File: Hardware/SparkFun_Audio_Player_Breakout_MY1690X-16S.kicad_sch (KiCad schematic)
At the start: 41 parts, among them J1 3.5mm TRRS, J2 Conn_01x03, J3 Conn_01x02, J4 USB_C_Receptacle, J5 Conn_01x06, J6 microSD, Q1 BSS138, U2 MY1690X-16S

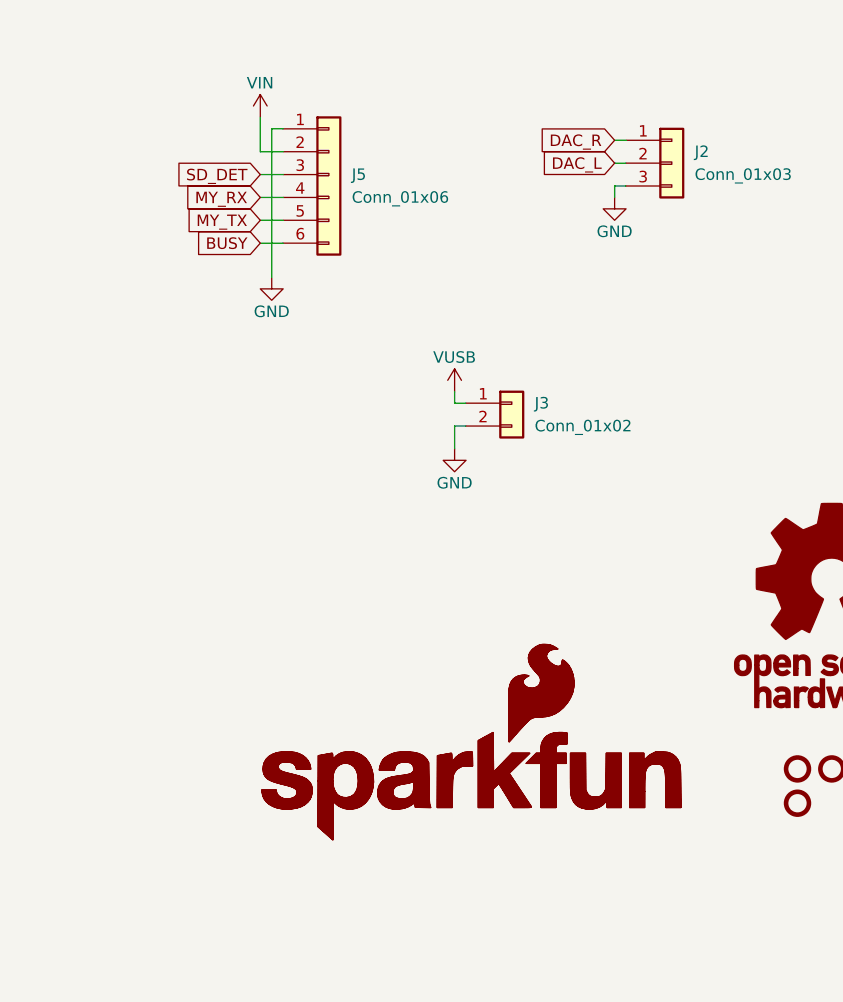
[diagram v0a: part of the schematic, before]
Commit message: re-order header pins to put GND/VIN/RX/TX in a row
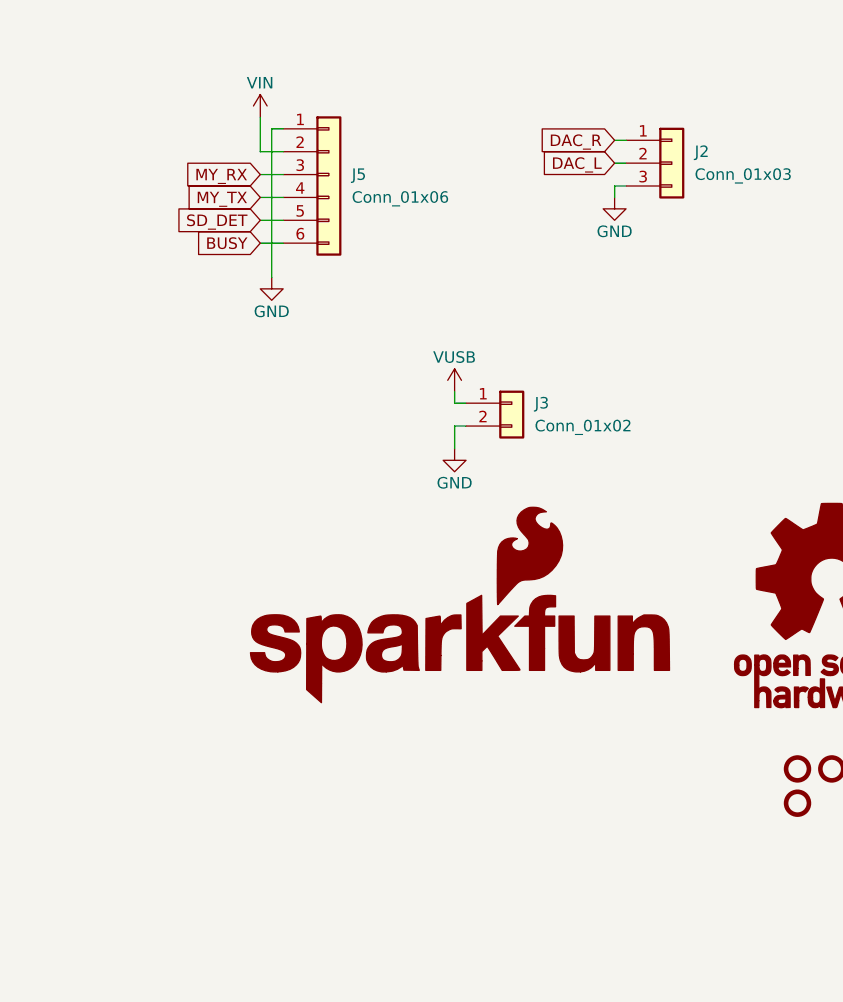
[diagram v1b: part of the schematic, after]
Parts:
- removed G3: SparkFun_Logo, symbol SparkFun-Aesthetic:SparkFun_Logo
- removed J1: 3.5mm TRRS, SparkFun-Connector:Audio_Jack_3.5mm_TRRS_SMD_RA, symbol SparkFun-Connector:Audio Jack TRRS 3.5mm SMD
- added J1: 3.5mm TRRS, SparkFun-Connector:Audio_Jack_3.5mm_TRRS_SMD_RA, symbol SparkFun-Connector:Audio_Jack_TRRS_3.5mm_SMD
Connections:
- net DAC_L: now also J1.T
- net DAC_R: now also J1.R1
- net GND: now also J1.R2
- net MY_RX: now also J5.3 (Pin_3); no longer J5.4 (Pin_4)
- net MY_TX: now also J5.4 (Pin_4); no longer J5.5 (Pin_5)
- net SD_DET: now also J5.5 (Pin_5); no longer J5.3 (Pin_3)
- net at JP3.1 (A): now also J1.S
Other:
- title: SparkFun Serial MP3 Player Shield -> SparkFun Audio Player Breakout MY1690X-16S
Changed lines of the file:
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@@
 	(paper "USLetter")
 	(title_block
-		(title "SparkFun Serial MP3 Player Shield")
-		(date "2025-01-17")
-		(rev "v11")
-		(comment 1 "Designed by: N. Seidle")
+		(title "SparkFun Audio Player Breakout MY1690X-16S")
+		(date "2025-01-24")
+		(rev "v01")
+		(comment 1 "Designed by: P. Lewis")
+		(comment 2 "Based on the MP3 Trigger Shield R3 by N. Seidle")
 	)
 	(junction
@@
 		)
 	)
+	(global_label "SD_DET"
+		(shape input)
+		(at 189.23 116.84 180)
+		(fields_autoplaced yes)
+		(effects
+			(font
+				(size 1.27 1.27)
+			)
+			(justify right)
+		)
+		(property "Intersheetrefs" "${INTERSHEET_REFS}"
+			(at 179.4111 116.84 0)
+			(effects
+				(font
+					(size 1.27 1.27)
+				)
+				(justify right)
+				(hide yes)
+			)
+		)
+	)
 	(global_label "MY_RX_LV"
 		(shape input)
@@
 		)
 	)
-	(global_label "SD_DET"
+	(global_label "MY_TX"
 		(shape input)
-		(at 189.23 111.76 180)
+		(at 189.23 114.3 180)
 		(fields_autoplaced yes)
 		(effects
@@
 		)
 		(property "Intersheetrefs" "${INTERSHEET_REFS}"
-			(at 179.4111 111.76 0)
+			(at 180.5601 114.3 0)
 			(effects
 				(font
@@
 	(global_label "MY_RX"
 		(shape input)
-		(at 189.23 114.3 180)
+		(at 189.23 111.76 180)
 		(fields_autoplaced yes)
 		(effects
@@
 		)
 		(property "Intersheetrefs" "${INTERSHEET_REFS}"
-			(at 180.2577 114.3 0)
+			(at 180.2577 111.76 0)
 			(effects
 				(font
@@
 		)
 	)
-	(global_label "MY_TX"
-		(shape input)
-		(at 189.23 116.84 180)
-		(fields_autoplaced yes)
-		(effects
-			(font
-				(size 1.27 1.27)
-			)
-			(justify right)
-		)
-		(property "Intersheetrefs" "${INTERSHEET_REFS}"
-			(at 180.5601 116.84 0)
-			(effects
-				(font
-					(size 1.27 1.27)
-				)
-				(justify right)
-				(hide yes)
-			)
-		)
-	)
 	(global_label "DAC_R"
 		(shape input)
@@
 	)
 	(symbol
+		(lib_id "SparkFun-Connector:Audio_Jack_TRRS_3.5mm_SMD")
+		(at 57.15 111.76 0)
+		(mirror y)
+		(unit 1)
+		(exclude_from_sim no)
+		(in_bom yes)
+		(on_board yes)
+		(dnp no)
+		(property "Reference" "J1"
+			(at 59.69 102.87 0)
+			(effects
+				(font
+					(size 1.27 1.27)
+				)
+			)
+		)
+		(property "Value" "3.5mm TRRS"
+			(at 59.69 105.41 0)
+			(effects
+				(font
+					(size 1.27 1.27)
+				)
+			)
+		)
+		(property "Footprint" "SparkFun-Connector:Audio_Jack_3.5mm_TRRS_SMD_RA"
+			(at 57.15 123.19 0)
+			(effects
+				(font
+					(size 1.27 1.27)
+				)
+				(hide yes)
+			)
+		)
+		(property "Datasheet" "https://cdn.sparkfun.com/datasheets/Prototyping/20153.pdf"
+			(at 57.15 120.65 0)
+			(effects
+				(font
+					(size 1.27 1.27)
+				)
+				(hide yes)
+			)
+		)
+		(property "Description" "Audio Jack, 4 Poles (TRRS)"
+			(at 57.15 125.73 0)
+			(effects
+				(font
+					(size 1.27 1.27)
+				)
+				(hide yes)
+			)
+		)
+		(property "PROD_ID" "CONN-10676"
+			(at 57.15 128.27 0)
+			(effects
+				(font
+					(size 1.27 1.27)
+				)
+				(hide yes)
+			)
+		)
+		(pin "S"
+		)
+		(pin "T"
+		)
+		(pin "R2"
+		)
+		(pin "R1"
+		)
+		(instances
+			(project ""
+				(path "/e3dd3ae4-244d-4cba-9cca-5d2abf83f29a"
+					(reference "J1")
+					(unit 1)
+				)
+			)
+		)
+	)
+	(symbol
 		(lib_id "SparkFun-PowerSymbol:3.3V_P")
 		(at 119.38 111.76 0)
@@
 	(symbol
 		(lib_id "SparkFun-Aesthetic:SparkFun_Logo")
-		(at 212.09 179.07 0)
+		(at 210.82 163.83 0)
 		(unit 1)
 		(exclude_from_sim no)
@@
 		(fields_autoplaced yes)
 		(property "Reference" "G5"
-			(at 212.09 172.72 0)
+			(at 210.82 157.48 0)
 			(effects
 				(font
@@
 		)
 		(property "Value" "SparkFun_Logo"
-			(at 212.09 184.15 0)
+			(at 210.82 168.91 0)
 			(effects
 				(font
@@
 		)
 		(property "Footprint" "SparkFun-Aesthetic:SparkFun_Logo_8mm"
-			(at 212.09 186.69 0)
+			(at 210.82 171.45 0)
 			(effects
 				(font
@@
 		)
 		(property "Datasheet" ""
-			(at 215.903 175.2712 0)
+			(at 214.633 160.0312 0)
 			(effects
 				(font
@@
 		)
 		(property "Description" ""
-			(at 212.09 179.07 0)
+			(at 210.82 163.83 0)
 			(effects
 				(font
@@
 	)
 	(symbol
-		(lib_id "SparkFun-Aesthetic:SparkFun_Logo")
-		(at 212.09 179.07 0)
-		(unit 1)
-		(exclude_from_sim no)
-		(in_bom yes)
-		(on_board no)
-		(dnp no)
-		(fields_autoplaced yes)
-		(property "Reference" "G3"
-			(at 212.09 172.72 0)
-			(effects
-				(font
-					(size 1.27 1.27)
-				)
-				(hide yes)
-			)
-		)
-		(property "Value" "SparkFun_Logo"
-			(at 212.09 184.15 0)
-			(effects
-				(font
-					(size 1.27 1.27)
-				)
-				(hide yes)
-			)
-		)
-		(property "Footprint" ""
-			(at 212.09 186.69 0)
-			(effects
-				(font
-					(size 1.27 1.27)
-				)
-				(hide yes)
-			)
-		)
-		(property "Datasheet" ""
-			(at 215.903 175.2712 0)
-			(effects
-				(font
-					(size 1.27 1.27)
-				)
-				(hide yes)
-			)
-		)
-		(property "Description" ""
-			(at 212.09 179.07 0)
-			(effects
-				(font
-					(size 1.27 1.27)
-				)
-				(hide yes)
-			)
-		)
-		(instances
-			(project "SparkFun_RTK_Postcard"
-				(path "/e3dd3ae4-244d-4cba-9cca-5d2abf83f29a"
-					(reference "G3")
-					(unit 1)
-				)
-			)
-		)
-	)
-	(symbol
 		(lib_id "SparkFun-Aesthetic:Fiducial_0.5mm")
 		(at 260.35 177.8 0)
@@
 					(unit 1)
 				)
-			)
-		)
-	)
-	(symbol
-		(lib_id "SparkFun-Connector:Audio Jack TRRS 3.5mm SMD")
-		(at 57.15 111.76 0)
-		(mirror y)
-		(unit 1)
-		(exclude_from_sim no)
-		(in_bom yes)
-		(on_board yes)
-		(dnp no)
-		(property "Reference" "J1"
-			(at 59.69 102.87 0)
-			(effects
-				(font
-					(size 1.27 1.27)
-				)
-			)
-		)
-		(property "Value" "3.5mm TRRS"
-			(at 59.69 105.41 0)
-			(effects
-				(font
-					(size 1.27 1.27)
-				)
-			)
-		)
-		(property "Footprint" "SparkFun-Connector:Audio_Jack_3.5mm_TRRS_SMD_RA"
-			(at 57.15 123.19 0)
-			(effects
-				(font
-					(size 1.27 1.27)
-				)
-				(hide yes)
-			)
-		)
-		(property "Datasheet" "https://cdn.sparkfun.com/datasheets/Prototyping/20153.pdf"
-			(at 57.15 120.65 0)
-			(effects
-				(font
-					(size 1.27 1.27)
-				)
-				(hide yes)
-			)
-		)
-		(property "Description" "Audio Jack, 4 Poles (TRRS)"
-			(at 57.15 125.73 0)
-			(effects
-				(font
-					(size 1.27 1.27)
-				)
-				(hide yes)
-			)
-		)
-		(property "PROD-ID" "CONN-10676"
-			(at 57.15 128.27 0)
-			(effects
-				(font
-					(size 1.27 1.27)
-				)
-				(hide yes)
-			)
-		)
-		(pin "R2"
-		)
-		(pin "S"
-		)
-		(pin "T"
-		)
-		(pin "R1"
-		)
-		(instances
-			(project ""
-				(path "/e3dd3ae4-244d-4cba-9cca-5d2abf83f29a"
-					(reference "J1")
-					(unit 1)
-				)

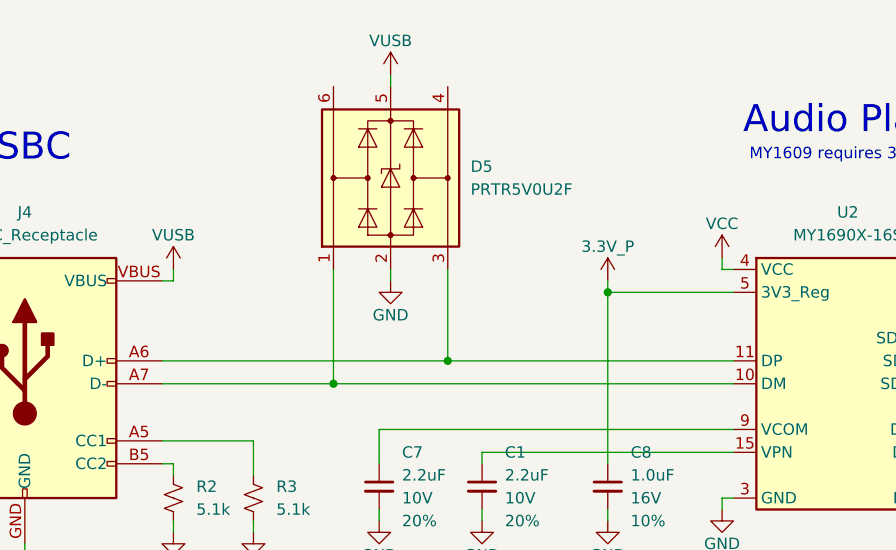
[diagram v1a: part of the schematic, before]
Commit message: TVS diode SOT23-6 package
-for easier production/rework
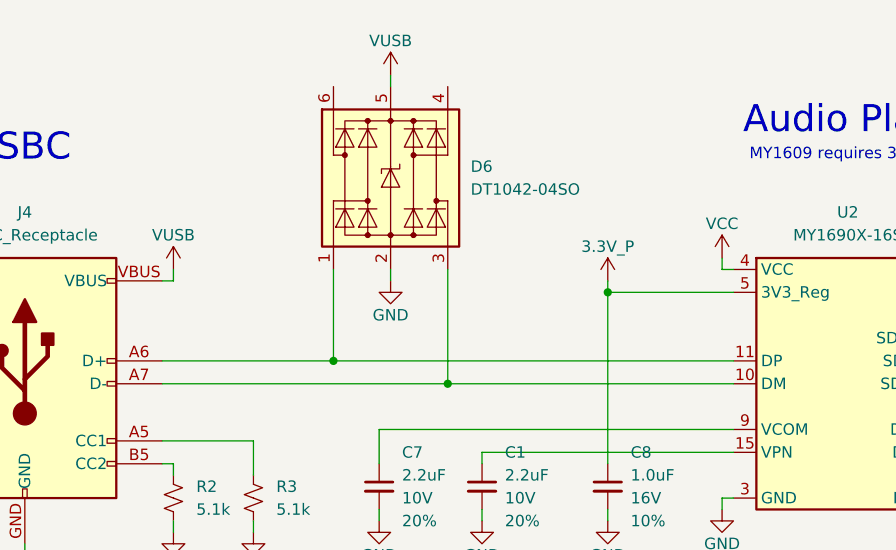
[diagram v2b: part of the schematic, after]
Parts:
- removed D5: PRTR5V0U2F, Package_TO_SOT_SMD:SOT-886, symbol SparkFun-DiscreteSemi:D_TVS_ESD_USB_SOT886
- added D6: DT1042-04SO, SparkFun-Semiconductor-Standard:SOT23-6, symbol SparkFun-DiscreteSemi:D_TVS_ESD_USB
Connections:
- net GND: now also D6.2 (GND)
- net VUSB: now also D6.5 (VCC)
- net at J4.A6 (D+), J4.B6 (D+), U2.11 (DP): now also D6.1 (I/O1)
- net at J4.A7 (D-), J4.B7 (D-), U2.10 (DM): now also D6.3 (I/O2)
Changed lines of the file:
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@@
 	)
 	(junction
-		(at 68.58 53.34)
+		(at 68.58 50.8)
 		(diameter 0)
 		(color 0 0 0 0)
@@
 	)
 	(junction
+		(at 81.28 53.34)
+		(diameter 0)
+		(color 0 0 0 0)
+	)
+	(junction
 		(at 119.38 120.65)
 		(diameter 0)
@@
 		(color 0 0 0 0)
 	)
-	(junction
-		(at 81.28 50.8)
-		(diameter 0)
-		(color 0 0 0 0)
-	)
 	(wire
 		(pts
@@
 	(wire
 		(pts
-			(xy 189.23 114.3) (xy 191.77 114.3)
+			(xy 49.53 50.8) (xy 68.58 50.8)
 		)
 		(stroke
@@
 	(wire
 		(pts
-			(xy 195.58 46.99) (xy 203.2 46.99)
+			(xy 189.23 114.3) (xy 191.77 114.3)
 		)
 		(stroke
@@
 	(wire
 		(pts
-			(xy 99.06 41.91) (xy 99.06 43.18)
+			(xy 195.58 46.99) (xy 203.2 46.99)
 		)
 		(stroke
@@
 	(wire
 		(pts
-			(xy 59.69 69.85) (xy 59.69 68.58)
+			(xy 99.06 41.91) (xy 99.06 43.18)
 		)
 		(stroke
@@
 	(wire
 		(pts
-			(xy 73.66 68.58) (xy 73.66 67.31)
+			(xy 59.69 69.85) (xy 59.69 68.58)
 		)
 		(stroke
@@
 	(wire
 		(pts
-			(xy 49.53 53.34) (xy 68.58 53.34)
+			(xy 73.66 68.58) (xy 73.66 67.31)
 		)
 		(stroke
@@
 	(wire
 		(pts
-			(xy 68.58 53.34) (xy 113.03 53.34)
+			(xy 49.53 53.34) (xy 81.28 53.34)
 		)
 		(stroke
@@
 	(wire
 		(pts
-			(xy 68.58 40.64) (xy 68.58 53.34)
-		)
-		(stroke
-			(width 0)
-			(type default)
-		)
-	)
-	(wire
-		(pts
-			(xy 49.53 50.8) (xy 81.28 50.8)
+			(xy 68.58 40.64) (xy 68.58 50.8)
 		)
 		(stroke
@@
 	(wire
 		(pts
-			(xy 81.28 50.8) (xy 113.03 50.8)
-		)
-		(stroke
-			(width 0)
-			(type default)
-		)
-	)
-	(wire
-		(pts
 			(xy 195.58 54.61) (xy 203.2 54.61)
 		)
@@
 	(wire
 		(pts
-			(xy 81.28 40.64) (xy 81.28 50.8)
+			(xy 190.5 106.68) (xy 190.5 123.19)
 		)
 		(stroke
@@
 	(wire
 		(pts
-			(xy 190.5 106.68) (xy 190.5 123.19)
+			(xy 81.28 40.64) (xy 81.28 53.34)
 		)
 		(stroke
@@
 	(wire
 		(pts
+			(xy 81.28 53.34) (xy 113.03 53.34)
+		)
+		(stroke
+			(width 0)
+			(type default)
+		)
+	)
+	(wire
+		(pts
 			(xy 156.21 58.42) (xy 162.56 58.42)
 		)
@@
 	(wire
 		(pts
+			(xy 68.58 50.8) (xy 113.03 50.8)
+		)
+		(stroke
+			(width 0)
+			(type default)
+		)
+	)
+	(wire
+		(pts
 			(xy 74.93 40.64) (xy 74.93 41.91)
 		)
@@
 	)
 	(symbol
+		(lib_id "SparkFun-DiscreteSemi:D_TVS_ESD_USB")
+		(at 74.93 29.21 0)
+		(unit 1)
+		(exclude_from_sim no)
+		(in_bom yes)
+		(on_board yes)
+		(dnp no)
+		(fields_autoplaced yes)
+		(property "Reference" "D6"
+			(at 83.82 29.2099 0)
+			(effects
+				(font
+					(size 1.27 1.27)
+				)
+				(justify left)
+			)
+		)
+		(property "Value" "DT1042-04SO"
+			(at 83.82 31.7499 0)
+			(effects
+				(font
+					(size 1.27 1.27)
+				)
+				(justify left)
+			)
+		)
+		(property "Footprint" "SparkFun-Semiconductor-Standard:SOT23-6"
+			(at 74.93 43.18 0)
+			(effects
+				(font
+					(size 1.27 1.27)
+				)
+				(hide yes)
+			)
+		)
+		(property "Datasheet" "https://www.diodes.com/assets/Datasheets/DT1042-04SO.pdf"
+			(at 74.93 45.72 0)
+			(effects
+				(font
+					(size 1.27 1.27)
+				)
+				(hide yes)
+			)
+		)
+		(property "Description" "Very low capacitance ESD protection diode, 4 data-line, SOT-23-6"
+			(at 75.184 50.8 0)
+			(effects
+				(font
+					(size 1.27 1.27)
+				)
+				(hide yes)
+			)
+		)
+		(property "PROD_ID" "IC-13538"
+			(at 74.93 48.26 0)
+			(effects
+				(font
+					(size 1.27 1.27)
+				)
+				(hide yes)
+			)
+		)
+		(pin "2"
+		)
+		(pin "3"
+		)
+		(pin "1"
+		)
+		(pin "4"
+		)
+		(pin "6"
+		)
+		(pin "5"
+		)
+		(instances
+			(project ""
+				(path "/e3dd3ae4-244d-4cba-9cca-5d2abf83f29a"
+					(reference "D6")
+					(unit 1)
+				)
+			)
+		)
+	)
+	(symbol
 		(lib_id "SparkFun-DiscreteSemi:Q_NMOS_0.2A_50V")
 		(at 125.73 118.11 270)
@@
 					(unit 1)
 				)
-			)
-		)
-	)
-	(symbol
-		(lib_id "SparkFun-DiscreteSemi:D_TVS_ESD_USB_SOT886")
-		(at 74.93 30.48 0)
-		(unit 1)
-		(exclude_from_sim no)
-		(in_bom yes)
-		(on_board yes)
-		(dnp no)
-		(fields_autoplaced yes)
-		(property "Reference" "D5"
-			(at 83.82 29.2099 0)
-			(effects
-				(font
-					(size 1.27 1.27)
-				)
-				(justify left)
-			)
-		)
-		(property "Value" "PRTR5V0U2F"
-			(at 83.82 31.7499 0)
-			(effects
-				(font
-					(size 1.27 1.27)
-				)
-				(justify left)
-			)
-		)
-		(property "Footprint" "Package_TO_SOT_SMD:SOT-886"
-			(at 74.93 43.18 0)
-			(effects
-				(font
-					(size 1.27 1.27)
-				)
-				(hide yes)
-			)
-		)
-		(property "Datasheet" "https://assets.nexperia.com/documents/data-sheet/PRTR5V0U2F_PRTR5V0U2K.pdf"
-			(at 74.93 45.72 0)
-			(effects
-				(font
-					(size 1.27 1.27)
-				)
-				(hide yes)
-			)
-		)
-		(property "Description" "Ultra low capacitance ESD protection diode, 2 data-line, SOT-886"
-			(at 73.914 50.292 0)
-			(effects
-				(font
-					(size 1.27 1.27)
-				)
-				(hide yes)
-			)
-		)
-		(property "PROD_ID" "DIO-14084"
-			(at 74.93 48.26 0)
-			(effects
-				(font
-					(size 1.27 1.27)
-				)
-				(hide yes)
-			)
-		)
-		(pin "4"
-		)
-		(pin "5"
-		)
-		(pin "2"
-		)
-		(pin "3"
-		)
-		(pin "1"
-		)
-		(pin "6"
-		)
-		(instances
-			(project ""
-				(path "/e3dd3ae4-244d-4cba-9cca-5d2abf83f29a"
-					(reference "D5")
-					(unit 1)
-				)

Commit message: Routed v01 (pre-review)
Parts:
- added C6: 10uF, SparkFun-Capacitor:C_0603_1608Metric, symbol SparkFun-Capacitor:10uF_0603_6.3V_20%
- added C9: 0.1uF, SparkFun-Capacitor:C_0603_1608Metric, symbol SparkFun-Capacitor:0.1uF_0603_25V_20%
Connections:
- net 3.3V_P: no longer JP2.2 (B)
- net GND: now also C6.2, C9.2
- net VCC: now also JP2.2 (B), C6.1, C9.1
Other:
- moved on the sheet: C2, C3, J6, R6
